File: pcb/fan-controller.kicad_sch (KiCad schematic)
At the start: 30 parts, among them J1 Barrel_Jack, J2 Conn_01x04_Pin, J3 Conn_01x04_Pin, J4 Conn_01x04_Pin, J5 Conn_01x04_Pin, J6 Conn_01x04_Pin, J7 Conn_01x04_Pin, Q1 2N7002, U2 AMS1117-5.0, U3 SHT4x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

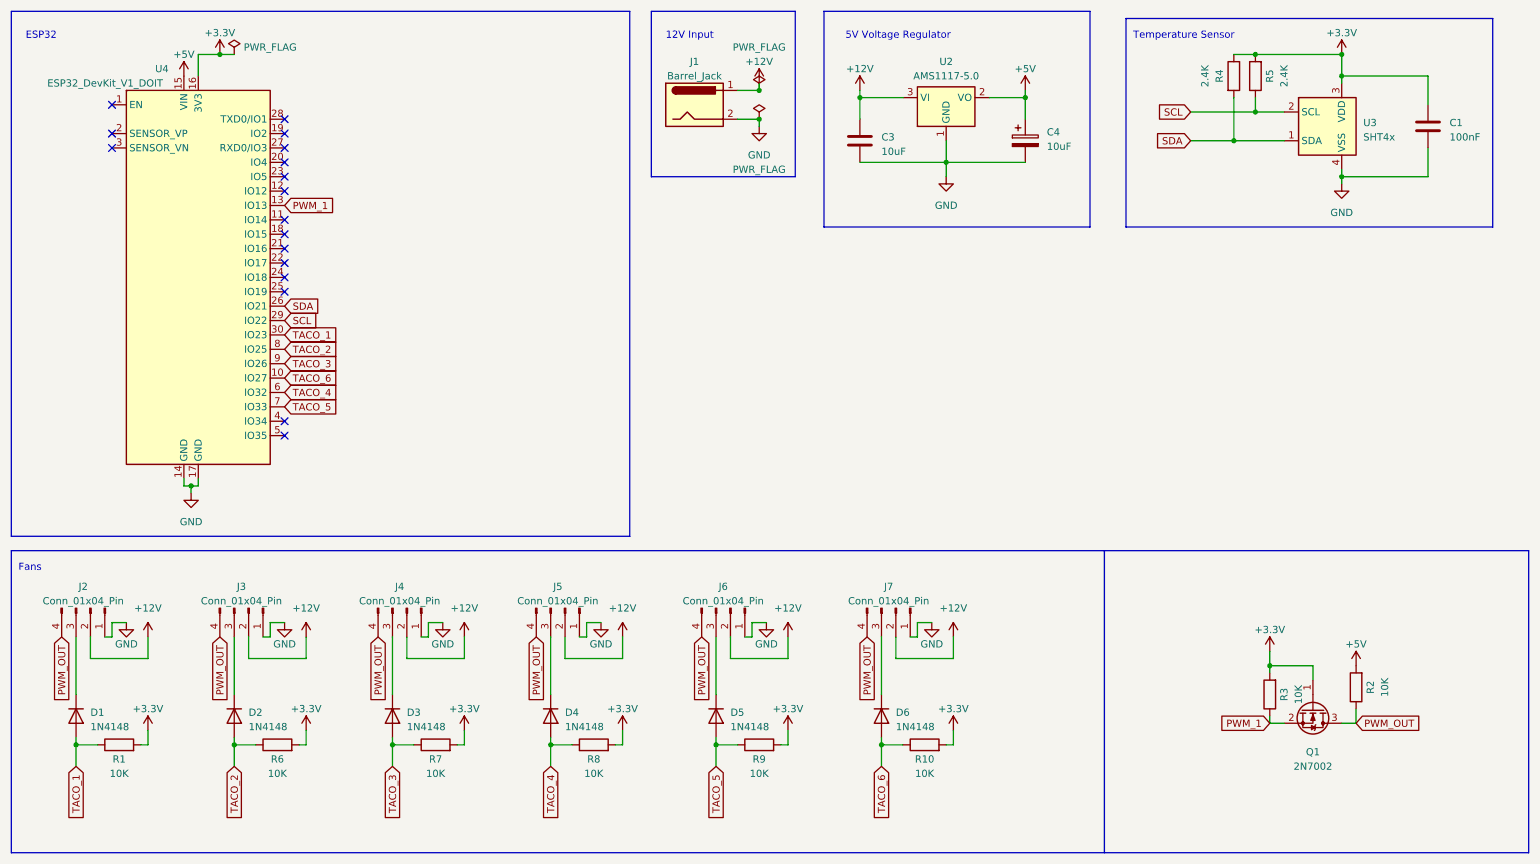
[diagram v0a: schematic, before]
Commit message: change voltage regulation
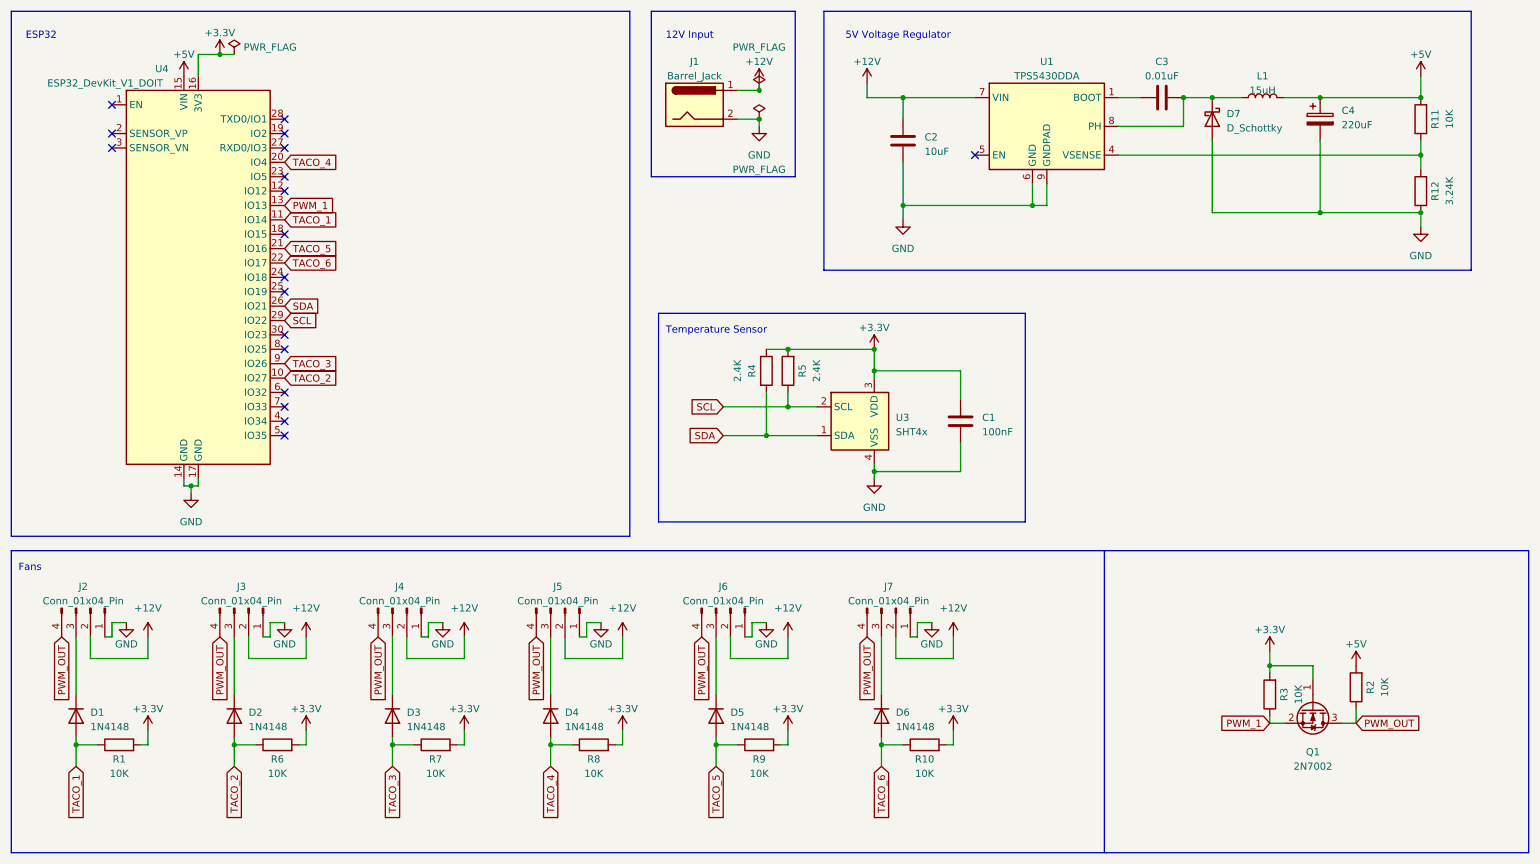
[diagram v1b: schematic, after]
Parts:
- removed U2: AMS1117-5.0, Package_TO_SOT_SMD:SOT-223-3_TabPin2, symbol Regulator_Linear:AMS1117-5.0
- added C2: 10uF, Capacitor_SMD:C_0603_1608Metric, symbol Device:C
- added D7: D_Schottky, Diode_SMD:D_SOD-123, symbol Device:D_Schottky
- added L1: 15uH, Inductor_SMD:L_1210_3225Metric, symbol Device:L
- added R11: 10K, Resistor_SMD:R_0603_1608Metric, symbol Device:R
- added R12: 3.24K, Resistor_SMD:R_0603_1608Metric, symbol Device:R
- added U1: TPS5430DDA, Package_SO:TI_SO-PowerPAD-8_ThermalVias, symbol Regulator_Switching:TPS5430DDA
- C3: value 10uF -> 0.01uF
- C4: value 10uF -> 220uF; footprint Capacitor_Tantalum_SMD:CP_EIA-3216-18_Kemet-A -> Capacitor_Tantalum_SMD:CP_EIA-3528-12_Kemet-T
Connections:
- net +12V: now also C2.1, U1.7 (VIN); no longer C3.1
- net +5V: now also L1.2, R11.2
- net GND: now also C2.2, D7.2 (A), R12.1, U1.6 (GND), U1.9 (GNDPAD); no longer C3.2
- net TACO_1: now also U4.11 (IO14); no longer U4.30 (IO23)
- net TACO_2: now also U4.10 (IO27); no longer U4.8 (IO25)
- net TACO_4: now also U4.20 (IO4); no longer U4.6 (IO32)
- net TACO_5: now also U4.21 (IO16); no longer U4.7 (IO33)
- net TACO_6: now also U4.22 (IO17); no longer U4.10 (IO27)
- new net: R11.1, R12.2, U1.4 (VSENSE)
- new net: C3.2, D7.1 (K), L1.1, U1.8 (PH)
- new net: C3.1, U1.1 (BOOT)
- no-connect marks 17 -> 18
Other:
- moved on the sheet: C1, R4, R5, U3
